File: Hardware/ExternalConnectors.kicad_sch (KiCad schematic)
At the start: 9 parts, among them J2 FTSH-105-X-X-DV-007-P-X, J4 A70-112-331N126, P1 USB_C_Plug_USB2.0

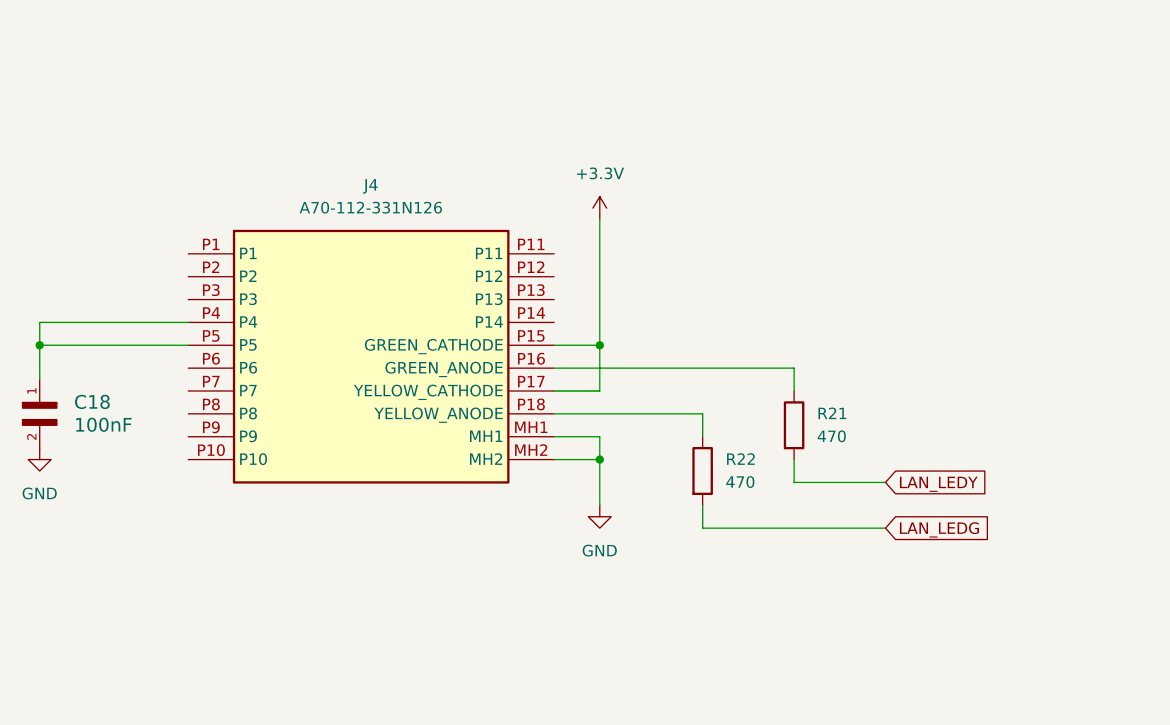
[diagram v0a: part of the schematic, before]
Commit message: Ethernet PHY and RJ45 connector
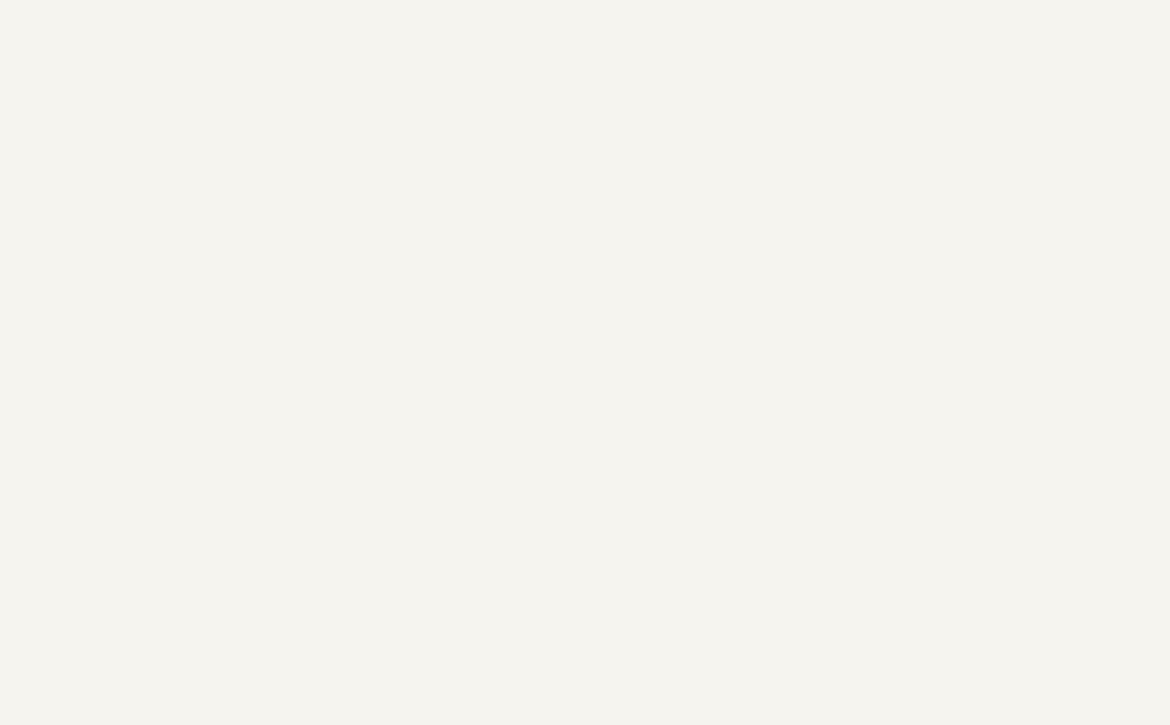
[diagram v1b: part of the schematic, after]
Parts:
- removed C18: 100nF, C0402C104J8RACTU:CAPC10555_55N_KEM-L, symbol 2025-06-22_21-59-05:C0402C104J8RACTU
- removed J4: A70-112-331N126, A70-112-331N126:A70112331N126, symbol A70-112-331N126:A70-112-331N126
- removed R21, R22: 470, Resistor_SMD:R_0402_1005Metric, symbol Device:R

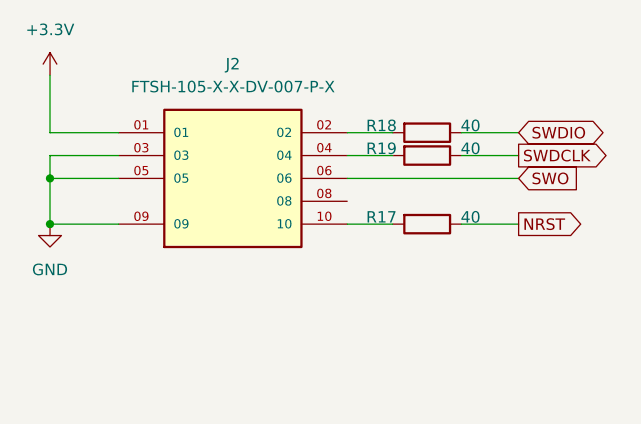
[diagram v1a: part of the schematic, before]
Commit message: Finished Ethernet connection between MAC and PHY
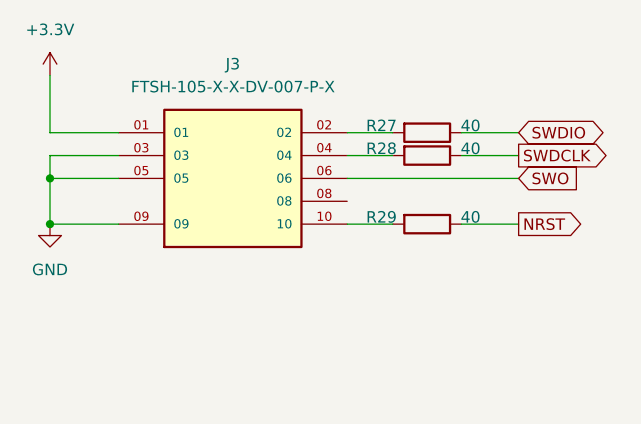
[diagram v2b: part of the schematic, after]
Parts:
- renumbered J2 to J3, R18 to R27, R19 to R28, R17 to R29
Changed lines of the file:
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@@
 		(on_board yes)
 		(dnp no)
-		(property "Reference" "R17"
+		(property "Reference" "R29"
 			(at 246.38 38.608 90)
 			(effects
@@
 			(project "Radio Project"
 				(path "/ca6389fe-9846-40e3-87a4-456cfcfc0777/d0c0b47f-61ad-4bb7-9e2d-9e0a26fbb87b"
-					(reference "R17")
+					(reference "R29")
 					(unit 1)
 				)
@@
 		(dnp no)
 		(fields_autoplaced yes)
-		(property "Reference" "#PWR022"
+		(property "Reference" "#PWR032"
 			(at 236.22 153.67 0)
 			(effects
@@
 			(project "Radio Project"
 				(path "/ca6389fe-9846-40e3-87a4-456cfcfc0777/d0c0b47f-61ad-4bb7-9e2d-9e0a26fbb87b"
-					(reference "#PWR022")
+					(reference "#PWR032")
 					(unit 1)
 				)
@@
 		(dnp no)
 		(fields_autoplaced yes)
-		(property "Reference" "#PWR021"
+		(property "Reference" "#PWR033"
 			(at 265.43 105.41 0)
 			(effects
@@
 			(project "Radio Project"
 				(path "/ca6389fe-9846-40e3-87a4-456cfcfc0777/d0c0b47f-61ad-4bb7-9e2d-9e0a26fbb87b"
-					(reference "#PWR021")
+					(reference "#PWR033")
 					(unit 1)
 				)
@@
 		(dnp no)
 		(fields_autoplaced yes)
-		(property "Reference" "J2"
+		(property "Reference" "J3"
 			(at 229.87 21.59 0)
 			(effects
@@
 			(project "Radio Project"
 				(path "/ca6389fe-9846-40e3-87a4-456cfcfc0777/d0c0b47f-61ad-4bb7-9e2d-9e0a26fbb87b"
-					(reference "J2")
+					(reference "J3")
 					(unit 1)
 				)
@@
 		(on_board yes)
 		(dnp no)
-		(property "Reference" "R18"
+		(property "Reference" "R27"
 			(at 246.38 28.448 90)
 			(effects
@@
 			(project "Radio Project"
 				(path "/ca6389fe-9846-40e3-87a4-456cfcfc0777/d0c0b47f-61ad-4bb7-9e2d-9e0a26fbb87b"
-					(reference "R18")
+					(reference "R27")
 					(unit 1)
 				)
@@
 		(on_board yes)
 		(dnp no)
-		(property "Reference" "R19"
+		(property "Reference" "R28"
 			(at 246.38 30.988 90)
 			(effects
@@
 			(project "Radio Project"
 				(path "/ca6389fe-9846-40e3-87a4-456cfcfc0777/d0c0b47f-61ad-4bb7-9e2d-9e0a26fbb87b"
-					(reference "R19")
+					(reference "R28")
 					(unit 1)
 				)
@@
 		(dnp no)
 		(fields_autoplaced yes)
-		(property "Reference" "#PWR07"
+		(property "Reference" "#PWR030"
 			(at 209.55 26.67 0)
 			(effects
@@
 			(project "Radio Project"
 				(path "/ca6389fe-9846-40e3-87a4-456cfcfc0777/d0c0b47f-61ad-4bb7-9e2d-9e0a26fbb87b"
-					(reference "#PWR07")
+					(reference "#PWR030")
 					(unit 1)
 				)
@@
 		(dnp no)
 		(fields_autoplaced yes)
-		(property "Reference" "#PWR08"
+		(property "Reference" "#PWR031"
 			(at 209.55 45.72 0)
 			(effects
@@
 			(project "Radio Project"
 				(path "/ca6389fe-9846-40e3-87a4-456cfcfc0777/d0c0b47f-61ad-4bb7-9e2d-9e0a26fbb87b"
-					(reference "#PWR08")
-					(unit 1)
-				)
+					(reference "#PWR031")
+					(unit 1)
+				)

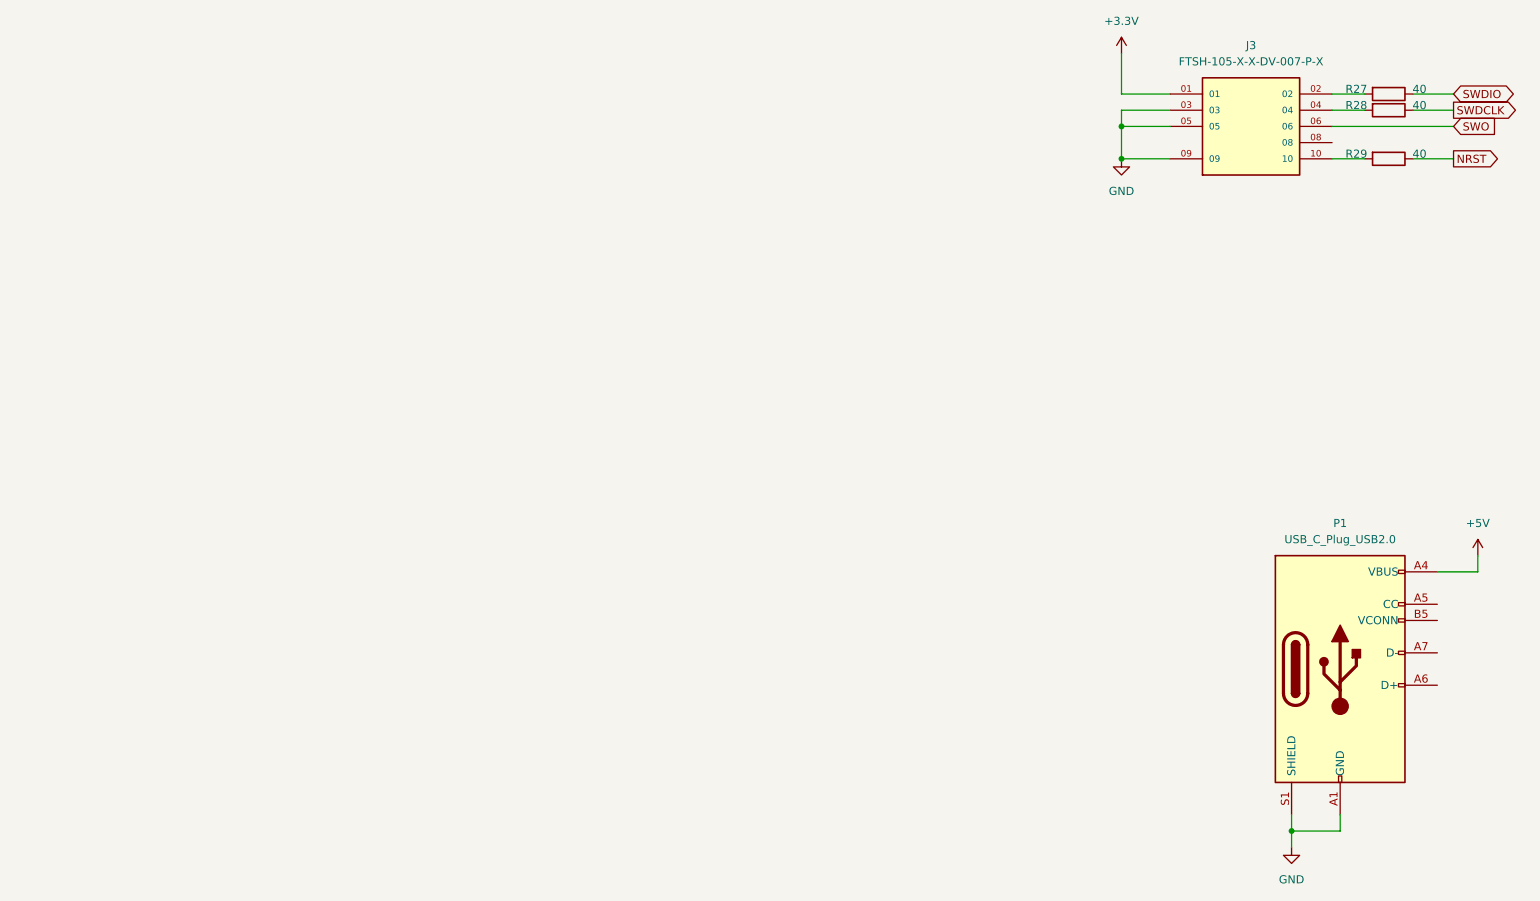
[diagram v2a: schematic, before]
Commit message: Added high power USB-C Connection (5V @ 3A)
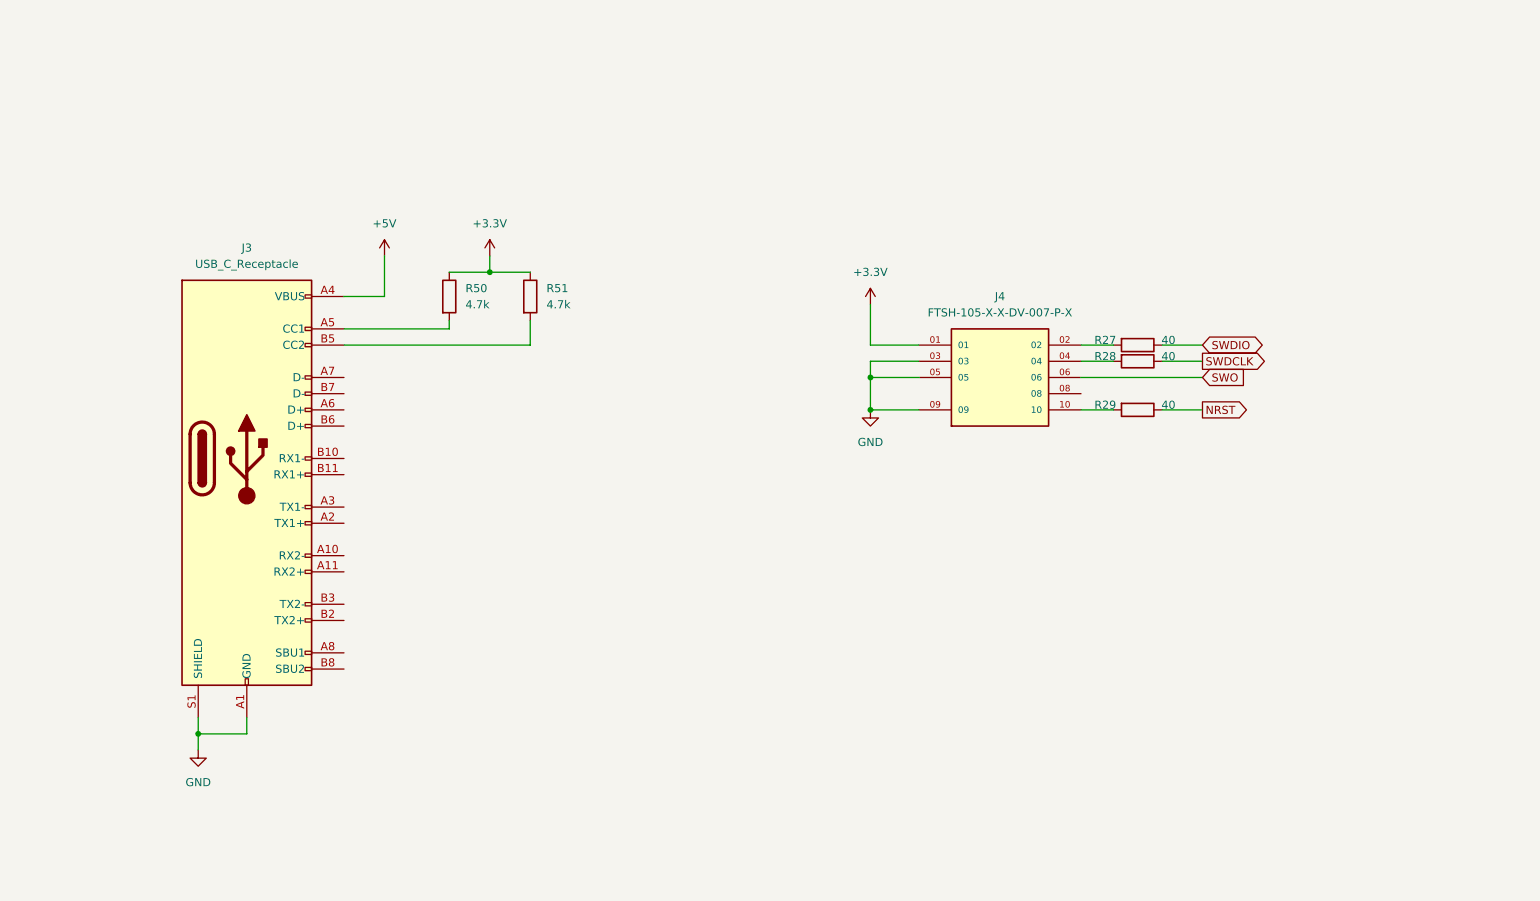
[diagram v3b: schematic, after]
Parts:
- removed P1: USB_C_Plug_USB2.0, Connector_USB:USB_C_Receptacle_GCT_USB4105-xx-A_16P_TopMnt_Horizontal, symbol Connector:USB_C_Plug_USB2.0
- added J3: USB_C_Receptacle, Connector_USB:USB_C_Receptacle_Amphenol_12401548E4-2A, symbol Connector:USB_C_Receptacle
- added R50, R51: 4.7k, Resistor_SMD:R_0402_1005Metric, symbol Device:R
- renumbered J3 to J4
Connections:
- net +3.3V: now also R50.1, R51.1
- net +5V: now also J3.A4 (VBUS), J3.A9 (VBUS), J3.B4 (VBUS), J3.B9 (VBUS)
- net GND: now also J3.A1 (GND), J3.A12 (GND), J3.B1 (GND), J3.B12 (GND), J3.S1 (SHIELD)
- new net: J3.A5 (CC1), R50.2
- new net: J3.B5 (CC2), R51.2
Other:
- moved on the sheet: J4, R27, R28, R29
